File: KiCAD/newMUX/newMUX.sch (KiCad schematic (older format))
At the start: 35 parts, among them J1 Conn_01x14, J2 Conn_02x06_Odd_Even, J3 Conn_02x06_Odd_Even, J4 Conn_01x14, U1 ASSR-1611, U10 ASSR-1611, U11 ASSR-1611, U12 ASSR-1611, U13 ASSR-1611, U14 ASSR-1611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

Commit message: new mux done
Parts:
- added L1: GREY@CHRISTOFORO.NET, myParts:logo, symbol GREY@CHRISTOFORO.NET
- C1: footprint (none) -> Capacitors_SMD:C_0603_HandSoldering
- J1, J4: footprint (none) -> Pin_Headers:Pin_Header_Straight_1x14_Pitch2.54mm
- J2, J3: footprint (none) -> Socket_Strips:Socket_Strip_Straight_2x06_Pitch2.54mm
- JP1, JP6: footprint (none) -> Connect:GS2
- JP2, JP3, JP4, JP5: footprint (none) -> Connect:GS3
- R1: footprint Resistors_SMD:R_0402 -> Resistors_SMD:R_2010_HandSoldering
- R2: footprint Resistors_SMD:R_0402 -> Resistors_SMD:R_0805_HandSoldering
- U22: footprint (none) -> Housings_DIP:DIP-28_W7.62mm
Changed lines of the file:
@@
 F 0 "U22" H 9850 3125 50  0000 R CNN
 F 1 "MCP23S17" H 9850 3050 50  0000 R CNN
-F 2 "" H 10000 1150 50  0001 L CNN
+F 2 "Housings_DIP:DIP-28_W7.62mm" H 10000 1150 50  0001 L CNN
 F 3 "" H 10200 3100 50  0001 C CNN
 	1    9950 2100
@@
 F 0 "J2" H 7200 5050 50  0000 C CNN
 F 1 "Conn_02x06_Odd_Even" H 7200 4350 50  0000 C CNN
-F 2 "" H 7150 4750 50  0001 C CNN
+F 2 "Socket_Strips:Socket_Strip_Straight_2x06_Pitch2.54mm" H 7150 4750 50  0001 C CNN
 F 3 "" H 7150 4750 50  0001 C CNN
 	1    7150 4750
@@
 F 0 "J3" H 8850 5050 50  0000 C CNN
 F 1 "Conn_02x06_Odd_Even" H 8850 4350 50  0000 C CNN
-F 2 "" H 8800 4750 50  0001 C CNN
+F 2 "Socket_Strips:Socket_Strip_Straight_2x06_Pitch2.54mm" H 8800 4750 50  0001 C CNN
 F 3 "" H 8800 4750 50  0001 C CNN
 	1    8800 4750
@@
 F 0 "C1" H 10925 1050 50  0000 L CNN
 F 1 "0.1uF" H 10925 850 50  0000 L CNN
-F 2 "" H 10938 800 50  0001 C CNN
+F 2 "Capacitors_SMD:C_0603_HandSoldering" H 10938 800 50  0001 C CNN
 F 3 "" H 10900 950 50  0001 C CNN
 	1    10900 950
@@
 F 0 "R1" V 3280 5350 50  0000 C CNN
 F 1 "830K" V 3200 5350 50  0000 C CNN
-F 2 "Resistors_SMD:R_0402" V 3130 5350 50  0001 C CNN
+F 2 "Resistors_SMD:R_2010_HandSoldering" V 3130 5350 50  0001 C CNN
 F 3 "" H 3200 5350 50  0000 C CNN
 	1    3200 5350
@@
 F 0 "J4" H 10900 6150 50  0000 C CNN
 F 1 "Conn_01x14" H 10900 4650 50  0000 C CNN
-F 2 "" H 10900 5450 50  0001 C CNN
+F 2 "Pin_Headers:Pin_Header_Straight_1x14_Pitch2.54mm" H 10900 5450 50  0001 C CNN
 F 3 "" H 10900 5450 50  0001 C CNN
 	1    10900 5450
@@
 F 0 "J1" H 750 7300 50  0000 C CNN
 F 1 "Conn_01x14" H 750 5800 50  0000 C CNN
-F 2 "" H 750 6600 50  0001 C CNN
+F 2 "Pin_Headers:Pin_Header_Straight_1x14_Pitch2.54mm" H 750 6600 50  0001 C CNN
 F 3 "" H 750 6600 50  0001 C CNN
 	1    750  6600
@@
 F 0 "R2" V 7580 1950 50  0000 C CNN
 F 1 "500K" V 7500 1950 50  0000 C CNN
-F 2 "Resistors_SMD:R_0402" V 7430 1950 50  0001 C CNN
+F 2 "Resistors_SMD:R_0805_HandSoldering" V 7430 1950 50  0001 C CNN
 F 3 "" H 7500 1950 50  0000 C CNN
 	1    7500 1950
@@
 F 0 "JP1" H 1400 6580 50  0000 C CNN
 F 1 "Jumper_NC_Small" H 1410 6440 50  0000 C CNN
-F 2 "" H 1400 6500 50  0001 C CNN
+F 2 "Connect:GS2" H 1400 6500 50  0001 C CNN
 F 3 "" H 1400 6500 50  0001 C CNN
 	1    1400 6500
@@
 F 0 "JP5" H 6650 6900 50  0000 L CNN
 F 1 "Jumper_NC_Dual" H 6600 7100 50  0000 C BNN
-F 2 "" H 6600 7000 50  0001 C CNN
+F 2 "Connect:GS3" H 6600 7000 50  0001 C CNN
 F 3 "" H 6600 7000 50  0001 C CNN
 	1    6600 7000
@@
 F 0 "JP4" H 6150 6900 50  0000 L CNN
 F 1 "Jumper_NC_Dual" H 6100 7100 50  0000 C BNN
-F 2 "" H 6100 7000 50  0001 C CNN
+F 2 "Connect:GS3" H 6100 7000 50  0001 C CNN
 F 3 "" H 6100 7000 50  0001 C CNN
 	1    6100 7000
@@
 F 0 "JP3" H 5750 6900 50  0000 L CNN
 F 1 "Jumper_NC_Dual" H 5700 7100 50  0000 C BNN
-F 2 "" H 5700 7000 50  0001 C CNN
+F 2 "Connect:GS3" H 5700 7000 50  0001 C CNN
 F 3 "" H 5700 7000 50  0001 C CNN
 	1    5700 7000
@@
 F 0 "JP2" H 5250 6900 50  0000 L CNN
 F 1 "Jumper_NC_Dual" H 5200 7100 50  0000 C BNN
-F 2 "" H 5200 7000 50  0001 C CNN
+F 2 "Connect:GS3" H 5200 7000 50  0001 C CNN
 F 3 "" H 5200 7000 50  0001 C CNN
 	1    5200 7000
@@
 F 0 "JP6" H 10250 5430 50  0000 C CNN
 F 1 "Jumper_NC_Small" H 10260 5290 50  0000 C CNN
-F 2 "" H 10250 5350 50  0001 C CNN
+F 2 "Connect:GS2" H 10250 5350 50  0001 C CNN
 F 3 "" H 10250 5350 50  0001 C CNN
 	1    10250 5350
@@
 Text Label 1450 4900 0    60   ~ 0
 VB
+$Comp
+L GREY@CHRISTOFORO.NET L1
+U 1 1 59B41702
+P 8950 7250
+F 0 "L1" H 8950 7125 60  0001 C CNN
+F 1 "GREY@CHRISTOFORO.NET" H 8950 7250 100 0000 C CNB
+F 2 "myParts:logo" H 8950 7250 60  0001 C CNN
+F 3 "" H 8950 7250 60  0001 C CNN
+	1    8950 7250
+	1    0    0    -1
+$EndComp
 $EndSCHEMATC

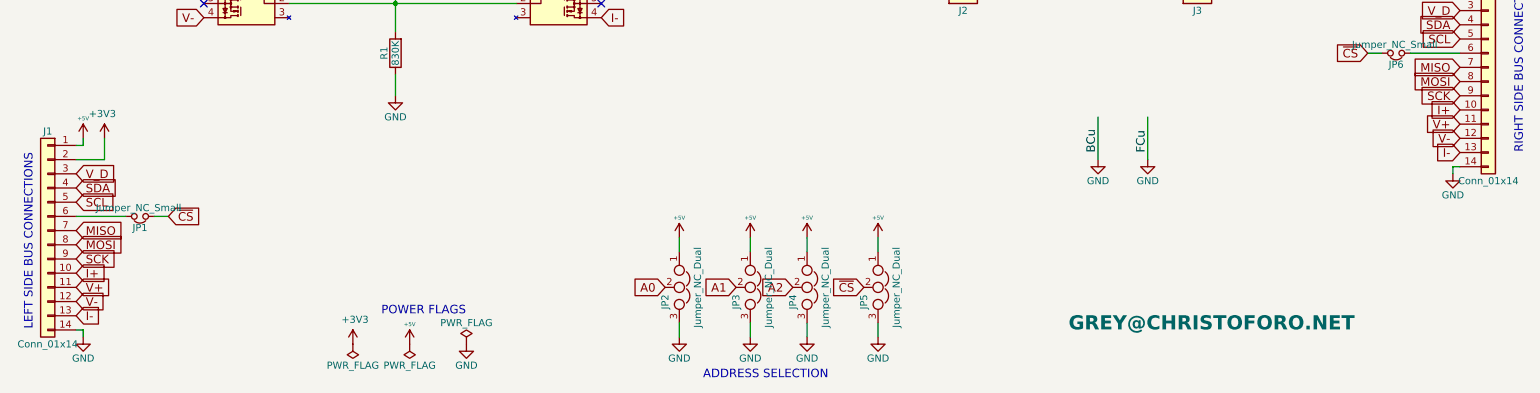
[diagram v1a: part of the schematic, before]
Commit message: fixed up newMux so that parts don't collide
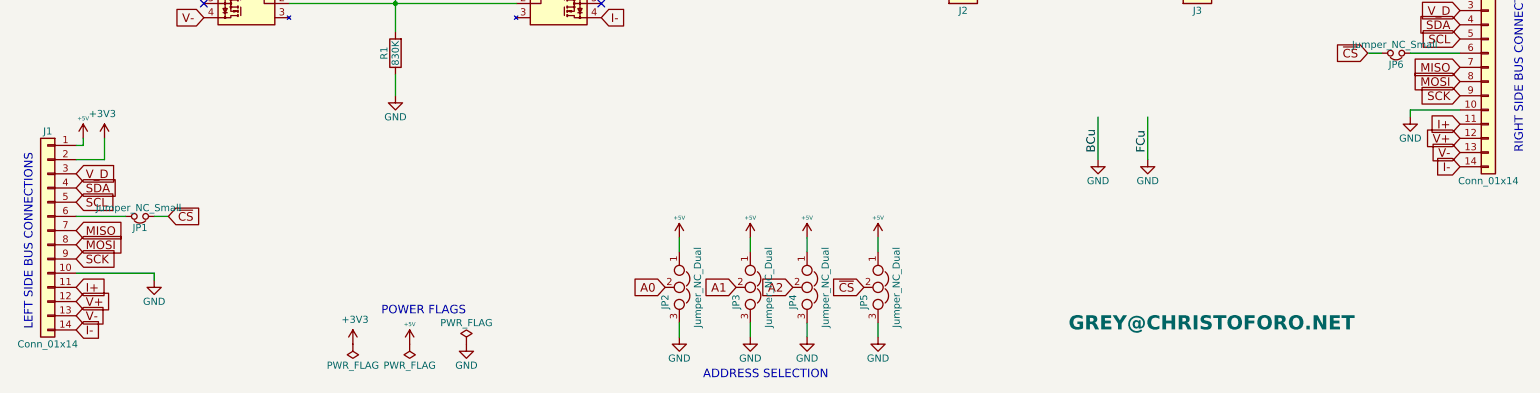
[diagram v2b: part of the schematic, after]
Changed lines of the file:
@@
 LIBS:valves
 LIBS:newMUX-cache
-EELAYER 25 0
+EELAYER 26 0
 EELAYER END
 $Descr A4 11693 8268
@@
 	1    0    0    -1
 $EndComp
+Text GLabel 10700 6050 0    60   Input ~ 0
+V-
+Text GLabel 10700 5850 0    60   Input ~ 0
+I+
+Text GLabel 10700 6150 0    60   Input ~ 0
+I-
 Text GLabel 10700 5950 0    60   Input ~ 0
-V-
-Text GLabel 10700 5750 0    60   Input ~ 0
-I+
-Text GLabel 10700 6050 0    60   Input ~ 0
-I-
-Text GLabel 10700 5850 0    60   Input ~ 0
 V+
 $Comp
 L GND #PWR018
 U 1 1 59B1E377
-P 10650 6200
-F 0 "#PWR018" H 10650 5950 50  0001 C CNN
-F 1 "GND" H 10650 6050 50  0000 C CNN
-F 2 "" H 10650 6200 50  0000 C CNN
-F 3 "" H 10650 6200 50  0000 C CNN
-	1    10650 6200
+P 10350 5800
+F 0 "#PWR018" H 10350 5550 50  0001 C CNN
+F 1 "GND" H 10350 5650 50  0000 C CNN
+F 2 "" H 10350 5800 50  0000 C CNN
+F 3 "" H 10350 5800 50  0000 C CNN
+	1    10350 5800
 	1    0    0    -1
 $EndComp
@@
 	10650 4850 10650 4800
 Wire Wire Line
-	10700 6150 10650 6150
-Wire Wire Line
-	10650 6150 10650 6200
+	10350 5750 10700 5750
+Wire Wire Line
+	10350 5750 10350 5800
 Wire Wire Line
 	10350 5350 10700 5350
@@
 Text GLabel 950  6800 2    60   Input ~ 0
 SCK
+Text GLabel 950  7200 2    60   Input ~ 0
+V-
+Text GLabel 950  7000 2    60   Input ~ 0
+I+
+Text GLabel 950  7300 2    60   Input ~ 0
+I-
 Text GLabel 950  7100 2    60   Input ~ 0
-V-
-Text GLabel 950  6900 2    60   Input ~ 0
-I+
-Text GLabel 950  7200 2    60   Input ~ 0
-I-
-Text GLabel 950  7000 2    60   Input ~ 0
 V+
 $Comp
 L GND #PWR022
 U 1 1 59B2F925
-P 1000 7350
-F 0 "#PWR022" H 1000 7100 50  0001 C CNN
-F 1 "GND" H 1000 7200 50  0000 C CNN
-F 2 "" H 1000 7350 50  0000 C CNN
-F 3 "" H 1000 7350 50  0000 C CNN
-	1    1000 7350
+P 1500 6950
+F 0 "#PWR022" H 1500 6700 50  0001 C CNN
+F 1 "GND" H 1500 6800 50  0000 C CNN
+F 2 "" H 1500 6950 50  0000 C CNN
+F 3 "" H 1500 6950 50  0000 C CNN
+	1    1500 6950
 	-1   0    0    -1
 $EndComp
@@
 	1000 6000 1000 5950
 Wire Wire Line
-	950  7300 1000 7300
-Wire Wire Line
-	1000 7300 1000 7350
+	950  6900 1500 6900
+Wire Wire Line
+	1500 6900 1500 6950
 Wire Wire Line
 	950  6500 1300 6500

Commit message: make spring pin board pin holders smaller, update base1x, update mux design controller board
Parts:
- added R3: 10K, Resistors_SMD:R_0805_HandSoldering, symbol R
- added RN1, RN2, RN3, RN4, RN5: 470R, Resistors_SMD:R_Cat16-4, symbol R_Pack04
- added TP1: Test_Point, myParts:Test_Point_S1751-46R, symbol Test_Point
- C1: footprint Capacitors_SMD:C_0603_HandSoldering -> Capacitors_SMD:C_0805_HandSoldering
- R1: value 830K -> 470R; footprint Resistors_SMD:R_2010_HandSoldering -> Resistors_SMD:R_0805_HandSoldering
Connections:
- net labels removed: PRE_GND
- wire segments 140 -> 195
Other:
- moved on the sheet: J1, JP1, JP2, JP3, JP4, JP5, R1, U1, U10, U11, U12, U13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

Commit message: wip commit
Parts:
- RN1, RN2, RN3, RN4, RN5: footprint Resistors_SMD:R_Cat16-4 -> myParts:VISHAY_CRA12E; farnellCode 2321730 -> 2352777
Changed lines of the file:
@@
 F 0 "RN1" H 2588 1046 50  0000 L CNN
 F 1 "470R" H 2588 955 50  0000 L CNN
-F 2 "Resistors_SMD:R_Cat16-4" V 2675 1000 50  0001 C CNN
+F 2 "myParts:VISHAY_CRA12E" V 2675 1000 50  0001 C CNN
 F 3 "" H 2400 1000 50  0001 C CNN
-F 4 "2321730" H 2400 1000 60  0001 C CNN "farnellCode"
+F 4 "2352777" H 2400 1000 60  0001 C CNN "farnellCode"
 	1    2400 1000
 	1    0    0    -1
@@
 F 0 "RN3" H 3138 1046 50  0000 L CNN
 F 1 "470R" H 3138 955 50  0000 L CNN
-F 2 "Resistors_SMD:R_Cat16-4" V 3225 1000 50  0001 C CNN
+F 2 "myParts:VISHAY_CRA12E" V 3225 1000 50  0001 C CNN
 F 3 "" H 2950 1000 50  0001 C CNN
-F 4 "2321730" H 2950 1000 60  0001 C CNN "farnellCode"
+F 4 "2352777" H 2950 1000 60  0001 C CNN "farnellCode"
 	1    2950 1000
 	1    0    0    -1
@@
 F 0 "RN4" H 3788 1046 50  0000 L CNN
 F 1 "470R" H 3788 955 50  0000 L CNN
-F 2 "Resistors_SMD:R_Cat16-4" V 3875 1000 50  0001 C CNN
+F 2 "myParts:VISHAY_CRA12E" V 3875 1000 50  0001 C CNN
 F 3 "" H 3600 1000 50  0001 C CNN
-F 4 "2321730" H 3600 1000 60  0001 C CNN "farnellCode"
+F 4 "2352777" H 3600 1000 60  0001 C CNN "farnellCode"
 	1    3600 1000
 	1    0    0    -1
@@
 F 0 "RN2" H 2588 6096 50  0000 L CNN
 F 1 "470R" H 2588 6005 50  0000 L CNN
-F 2 "Resistors_SMD:R_Cat16-4" V 2675 6050 50  0001 C CNN
+F 2 "myParts:VISHAY_CRA12E" V 2675 6050 50  0001 C CNN
 F 3 "" H 2400 6050 50  0001 C CNN
-F 4 "2321730" H 2400 6050 60  0001 C CNN "farnellCode"
+F 4 "2352777" H 2400 6050 60  0001 C CNN "farnellCode"
 	1    2400 6050
 	1    0    0    -1
@@
 F 0 "RN5" H 3788 6046 50  0000 L CNN
 F 1 "470R" H 3788 5955 50  0000 L CNN
-F 2 "Resistors_SMD:R_Cat16-4" V 3875 6000 50  0001 C CNN
+F 2 "myParts:VISHAY_CRA12E" V 3875 6000 50  0001 C CNN
 F 3 "" H 3600 6000 50  0001 C CNN
-F 4 "2321730" H 3600 6000 60  0001 C CNN "farnellCode"
+F 4 "2352777" H 3600 6000 60  0001 C CNN "farnellCode"
 	1    3600 6000
 	1    0    0    -1

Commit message: rotate connectors on newMux
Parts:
- C1: symbol C -> device:C
- J1, J4: symbol Conn_01x14 -> Connector:Conn_01x14
- J2, J3: symbol Conn_02x06_Odd_Even -> Connector:Conn_02x06_Odd_Even
- JP1, JP6: symbol Jumper_NC_Small -> device:Jumper_NC_Small
- JP2, JP3, JP4, JP5: symbol Jumper_NC_Dual -> device:Jumper_NC_Dual
- L1: symbol GREY@CHRISTOFORO.NET -> myParts:GREY@CHRISTOFORO.NET
- R1, R2, R3: symbol R -> device:R
- RN1, RN2, RN3, RN4, RN5: symbol R_Pack04 -> device:R_Pack04
- TP1: symbol Test_Point -> Connector:Test_Point
- U1, U10, U11, U12, U13, U14, U15, U16, U17, U18, U19, U2, U20, U21, U3, U4, U5, U6, U7, U8, U9: symbol ASSR-1611 -> myParts:ASSR-1611
- U22: symbol MCP23S17 -> microchip:MCP23S17
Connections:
- wire segments 195 -> 229

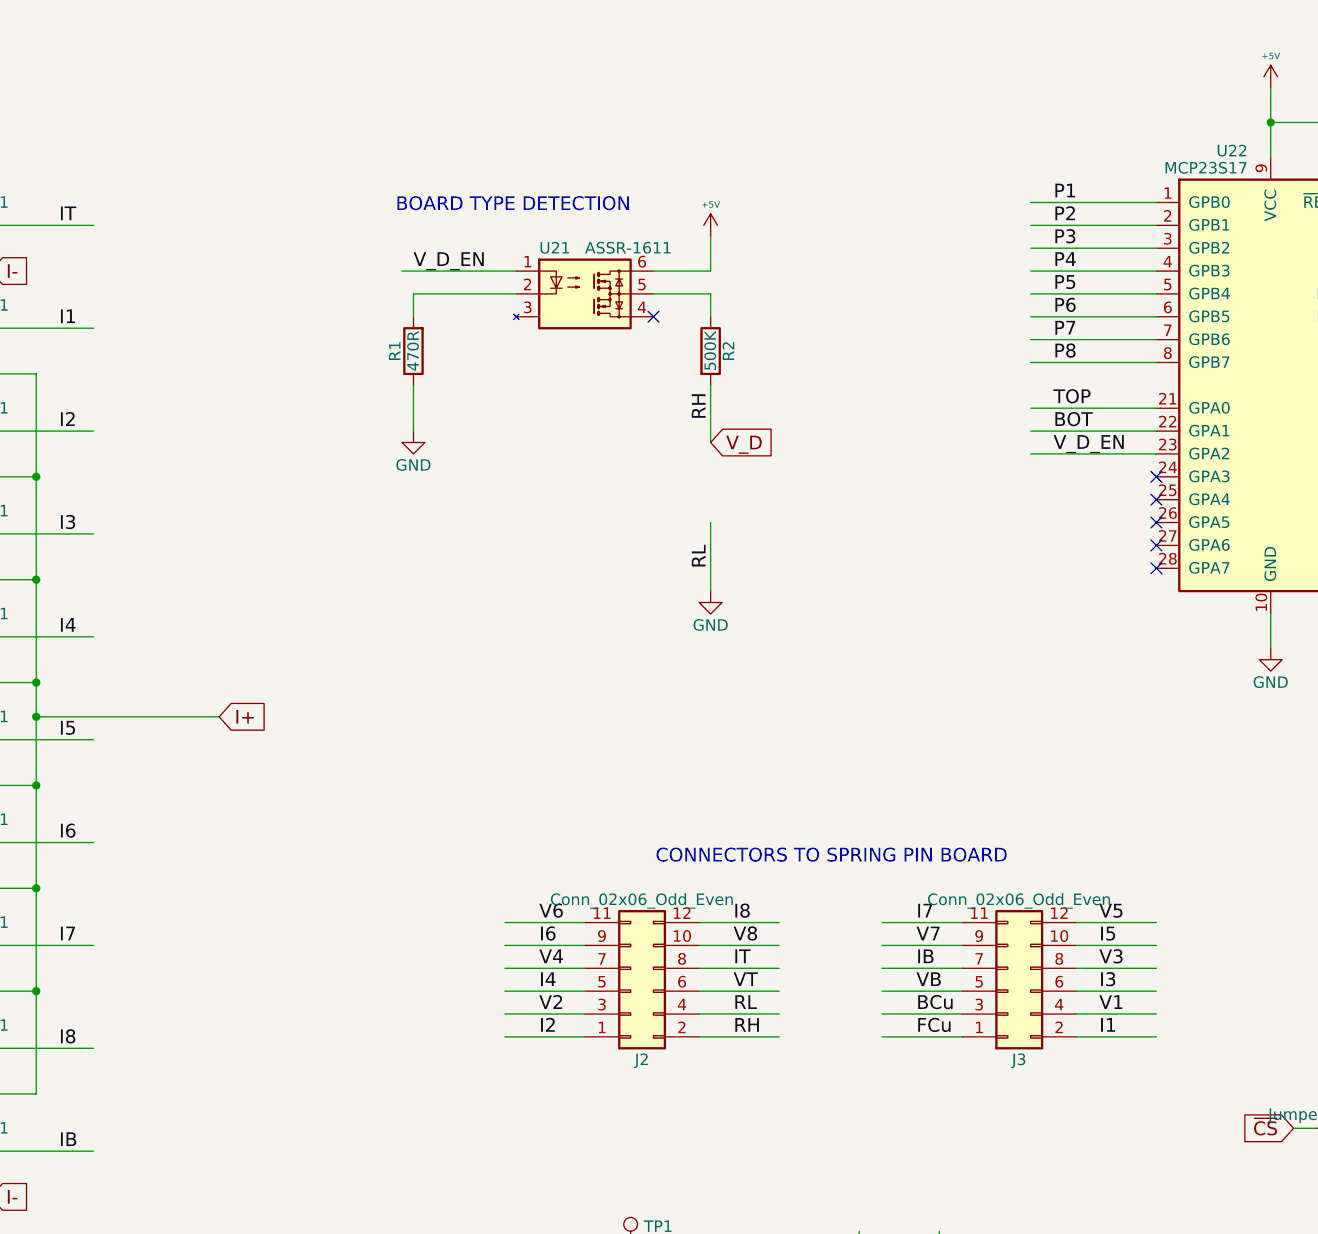
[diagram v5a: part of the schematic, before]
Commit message: rotate connectors on base1x
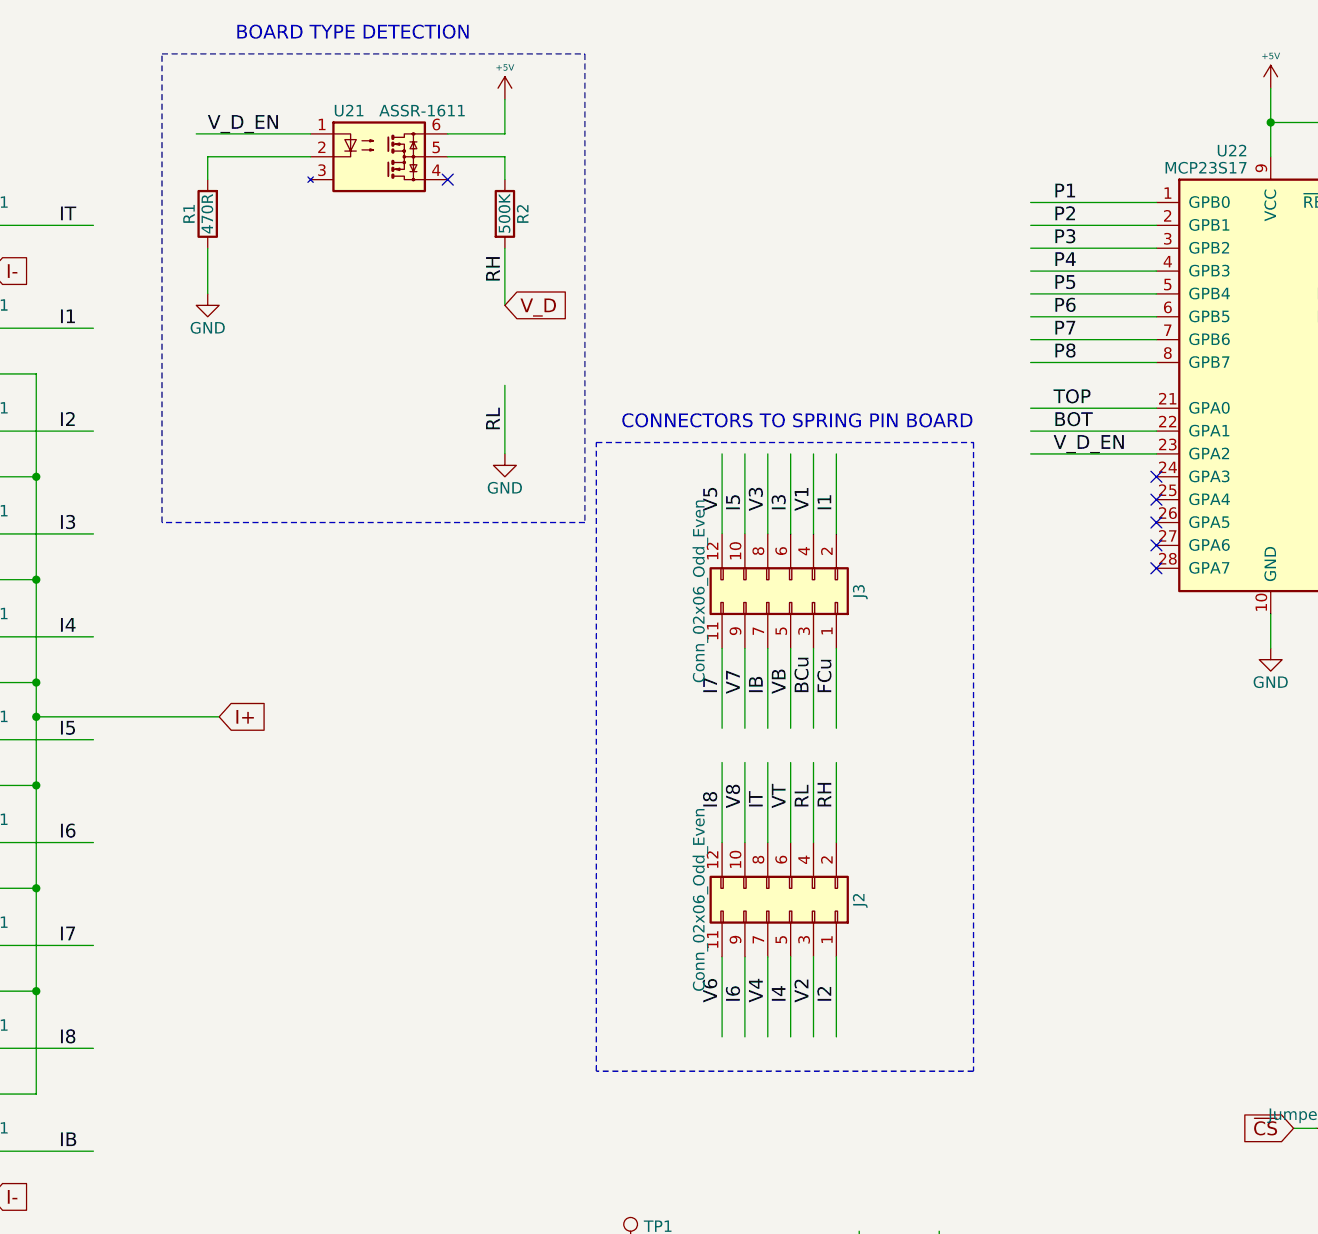
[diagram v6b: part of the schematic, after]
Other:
- moved on the sheet: J2, J3, R1, R2, U21
